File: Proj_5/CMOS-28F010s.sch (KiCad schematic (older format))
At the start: 5 parts, among them U12 28F010, U13 PAL16L8, U4 28F010

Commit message: Sick wires bro
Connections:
- net A17: now also U13.3 (I3); no longer U13.17 (I03)
- net A18: now also U13.2 (I2); no longer U13.18 (IO2)
- net A19: now also U13.1 (I1); no longer U13.19 (IO1)
- net ~BHE: now also U13.5 (I5); no longer U13.15 (IO5)
- net ~BLE: now also U13.4 (I4); no longer U13.16 (IO4)
- net at U12.22 (CE): now also U13.18 (IO2); no longer U13.2 (I2)
- net at U4.22 (CE): now also U13.19 (IO1); no longer U13.1 (I1)
- net M~IO: now reaches U13.6 (I6)
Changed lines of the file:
@@
 $Descr User 15748 23622
 encoding utf-8
-Sheet 8 9
+Sheet 7 9
 Title ""
 Date ""
@@
 F 3 "" H 10350 4550 50  0001 C CNN
 	1    10350 4550
-	1    0    0    -1
+	-1   0    0    -1
 $EndComp
 Text HLabel 10850 4050 2    50   Input ~ 0
@@
 Text HLabel 7350 2900 2    50   Input ~ 0
 A14
+Text HLabel 10850 4550 2    50   Input ~ 0
+M~IO
 $EndSCHEMATC

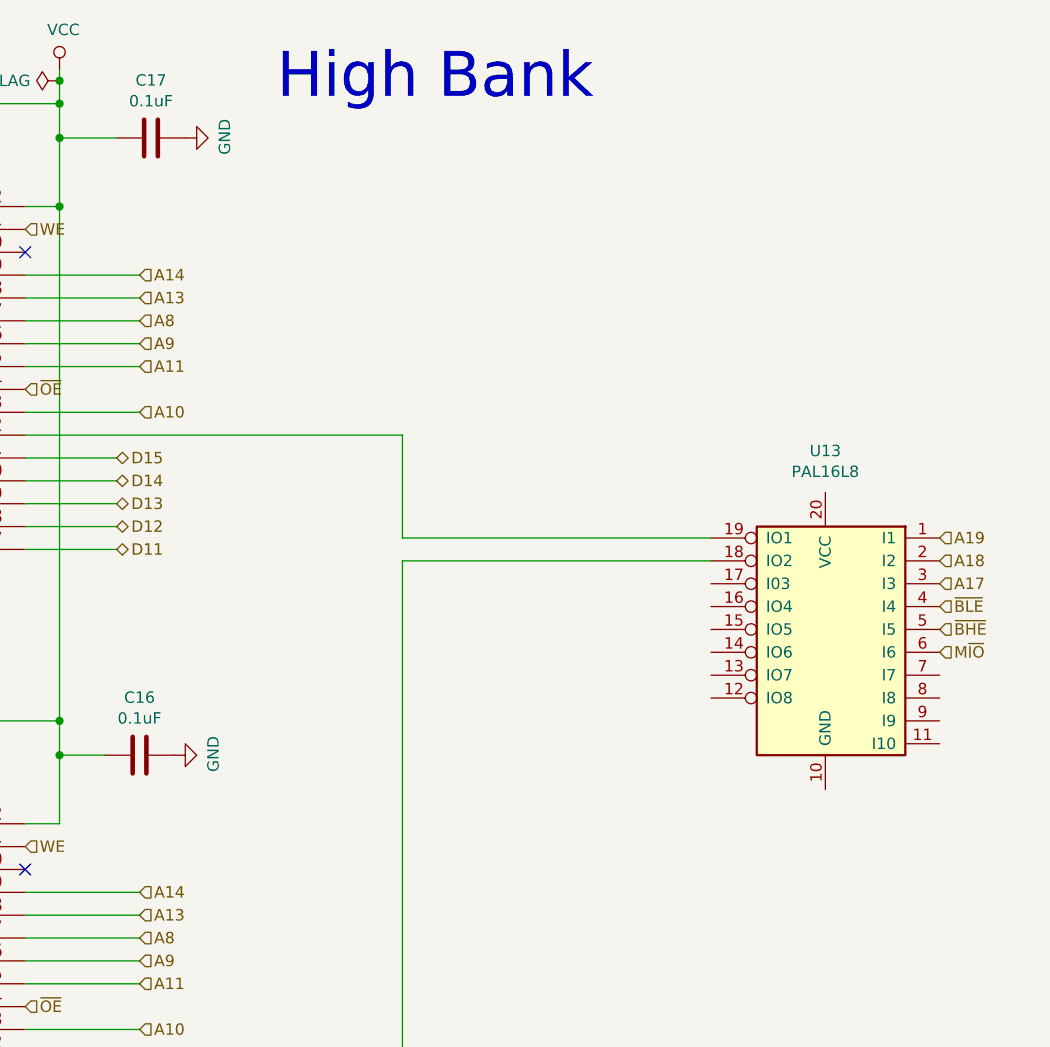
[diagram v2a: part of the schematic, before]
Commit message: Added Power Flags, finished no connects.
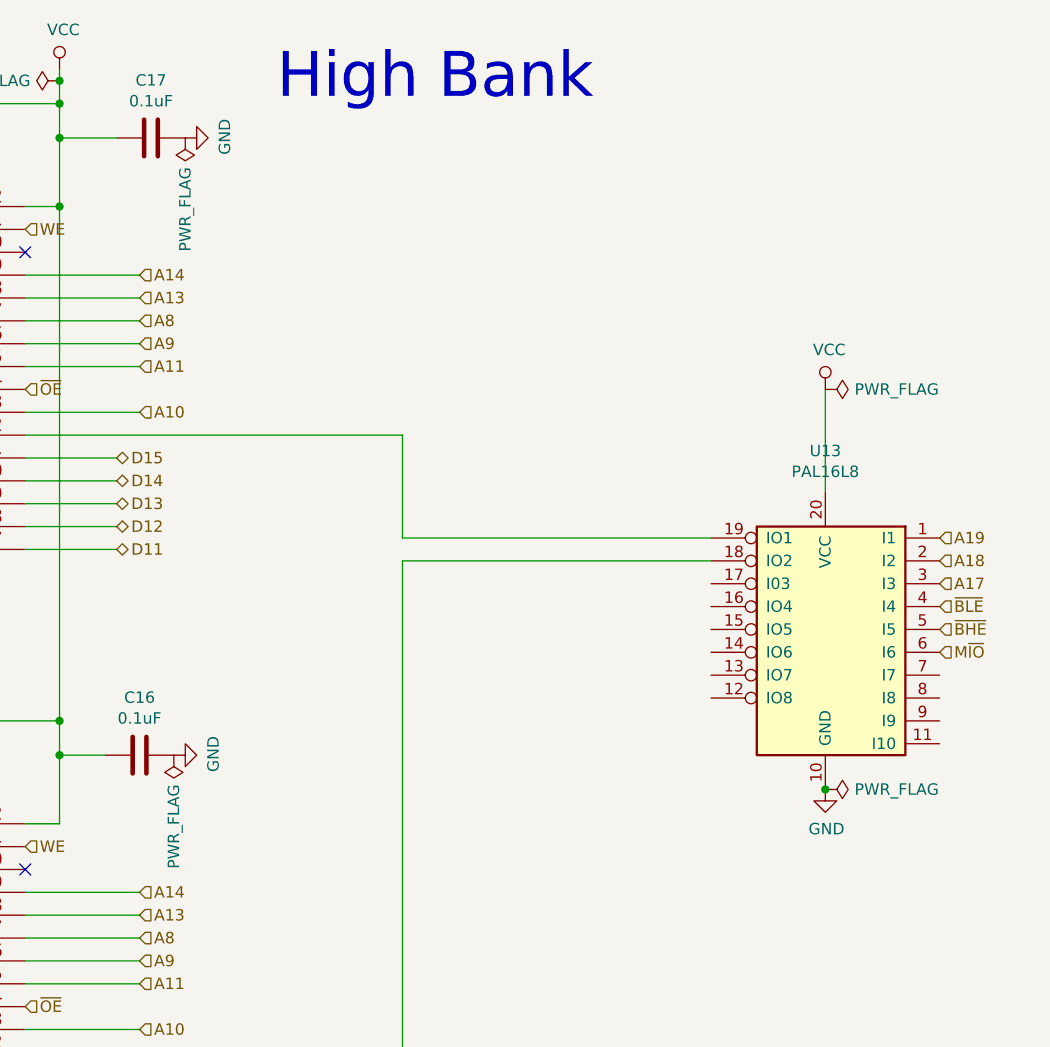
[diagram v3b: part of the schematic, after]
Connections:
- net GND: now also U13.10 (GND)
- net VCC: now also U13.20 (VCC)
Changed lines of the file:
@@
 $Descr User 15748 23622
 encoding utf-8
-Sheet 5 9
+Sheet 5 10
 Title ""
 Date ""
@@
 Text HLabel 10850 4550 2    50   Input ~ 0
 M~IO
+$Comp
+L power:PWR_FLAG #FLG?
+U 1 1 5F396526
+P 7500 5000
+AR Path="/5EAF7226/5F396526" Ref="#FLG?"  Part="1"
+AR Path="/5EA045EA/5F396526" Ref="#FLG041"  Part="1"
+F 0 "#FLG041" H 7500 5075 50  0001 C CNN
+F 1 "PWR_FLAG" V 7500 5128 50  0000 L CNN
+F 2 "" H 7500 5000 50  0001 C CNN
+F 3 "~" H 7500 5000 50  0001 C CNN
+	1    7500 5000
+	-1   0    0    1
+$EndComp
+$Comp
+L power:PWR_FLAG #FLG?
+U 1 1 5F398AC0
+P 7550 2300
+AR Path="/5EAF7226/5F398AC0" Ref="#FLG?"  Part="1"
+AR Path="/5EA045EA/5F398AC0" Ref="#FLG042"  Part="1"
+F 0 "#FLG042" H 7550 2375 50  0001 C CNN
+F 1 "PWR_FLAG" V 7550 2428 50  0000 L CNN
+F 2 "" H 7550 2300 50  0001 C CNN
+F 3 "~" H 7550 2300 50  0001 C CNN
+	1    7550 2300
+	-1   0    0    1
+$EndComp
+$Comp
+L power:PWR_FLAG #FLG?
+U 1 1 5F39F13F
+P 10350 5150
+AR Path="/5EAF7226/5F39F13F" Ref="#FLG?"  Part="1"
+AR Path="/5EA045EA/5F39F13F" Ref="#FLG044"  Part="1"
+F 0 "#FLG044" H 10350 5225 50  0001 C CNN
+F 1 "PWR_FLAG" V 10350 5278 50  0000 L CNN
+F 2 "" H 10350 5150 50  0001 C CNN
+F 3 "~" H 10350 5150 50  0001 C CNN
+	1    10350 5150
+	0    1    1    0
+$EndComp
+$Comp
+L power:GND #PWR047
+U 1 1 5F3A169C
+P 10350 5150
+AR Path="/5EA045EA/5F3A169C" Ref="#PWR047"  Part="1"
+AR Path="/5EA98353/5EA34234/5F3A169C" Ref="#PWR?"  Part="1"
+F 0 "#PWR047" H 10350 4900 50  0001 C CNN
+F 1 "GND" H 10355 4977 50  0000 C CNN
+F 2 "" H 10350 5150 50  0001 C CNN
+F 3 "" H 10350 5150 50  0001 C CNN
+	1    10350 5150
+	1    0    0    -1
+$EndComp
+Connection ~ 10350 5150
+$Comp
+L power:VCC #PWR046
+U 1 1 5F3AB457
+P 10350 3400
+AR Path="/5EA045EA/5F3AB457" Ref="#PWR046"  Part="1"
+AR Path="/5EA98353/5EA34234/5F3AB457" Ref="#PWR?"  Part="1"
+F 0 "#PWR046" H 10350 3250 50  0001 C CNN
+F 1 "VCC" H 10367 3573 50  0000 C CNN
+F 2 "" H 10350 3400 50  0001 C CNN
+F 3 "" H 10350 3400 50  0001 C CNN
+	1    10350 3400
+	1    0    0    -1
+$EndComp
+Wire Wire Line
+	10350 3400 10350 3850
+$Comp
+L power:PWR_FLAG #FLG?
+U 1 1 5F3B0971
+P 10350 3400
+AR Path="/5EAF7226/5F3B0971" Ref="#FLG?"  Part="1"
+AR Path="/5EA045EA/5F3B0971" Ref="#FLG043"  Part="1"
+F 0 "#FLG043" H 10350 3475 50  0001 C CNN
+F 1 "PWR_FLAG" V 10350 3528 50  0000 L CNN
+F 2 "" H 10350 3400 50  0001 C CNN
+F 3 "~" H 10350 3400 50  0001 C CNN
+	1    10350 3400
+	0    1    1    0
+$EndComp
 $EndSCHEMATC

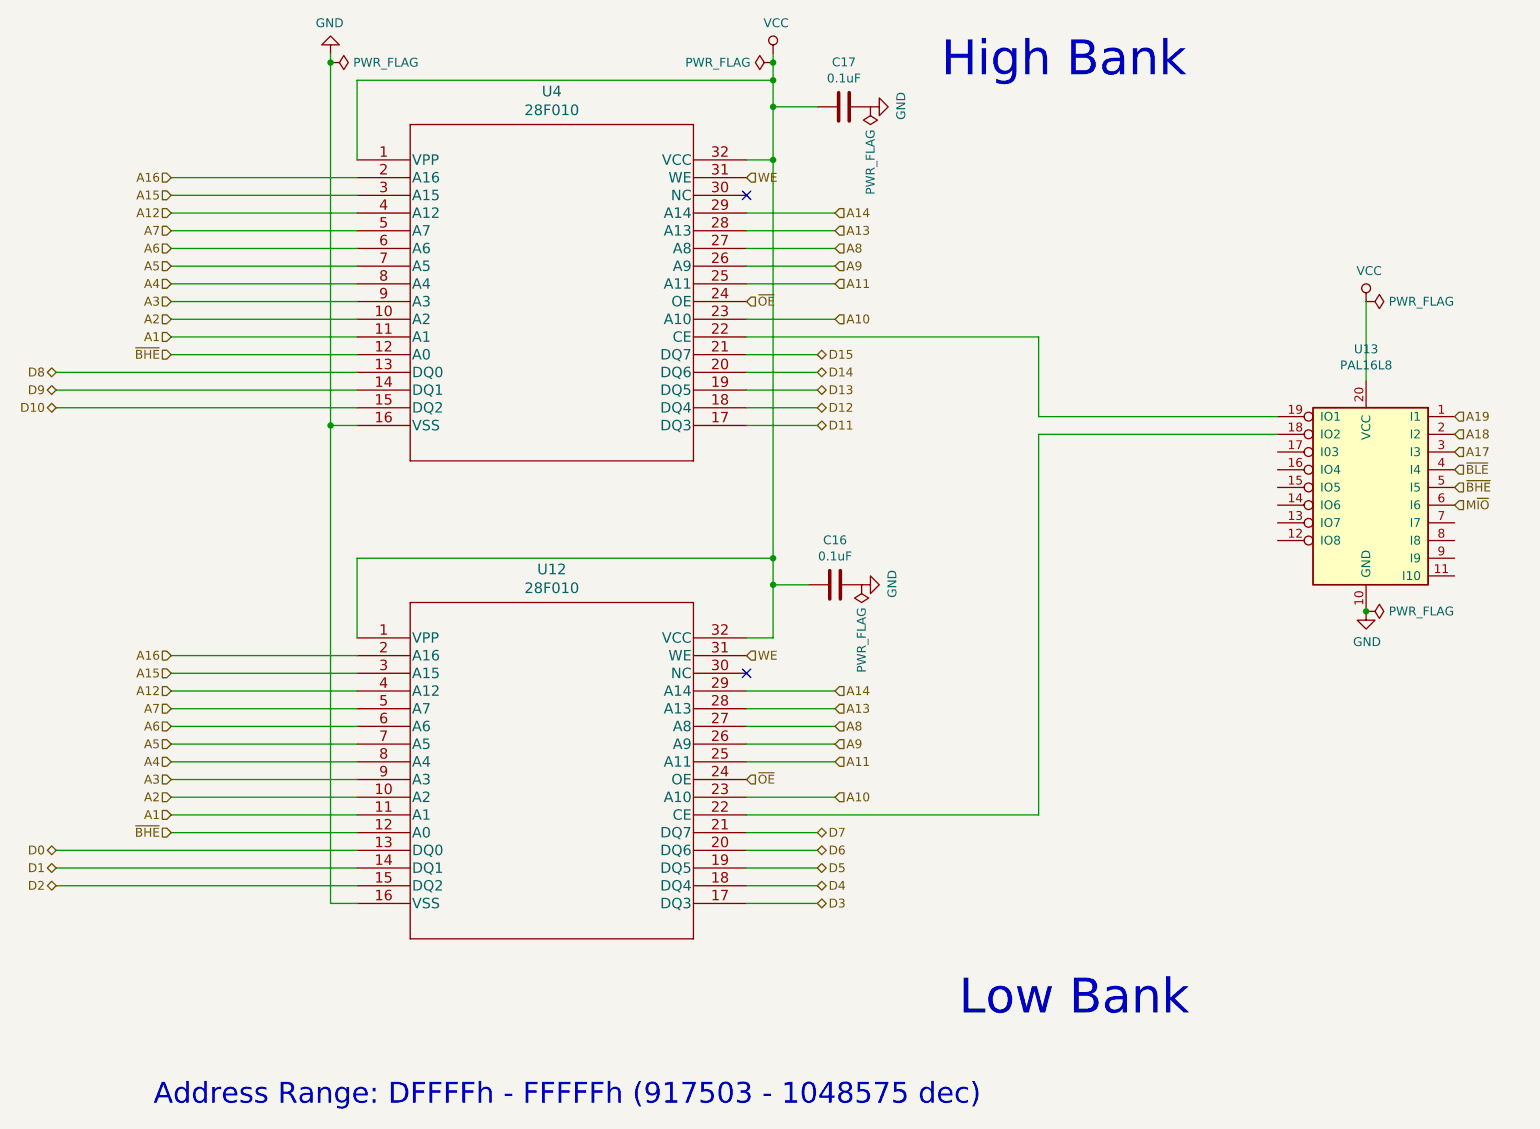
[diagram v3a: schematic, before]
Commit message: Power Flags
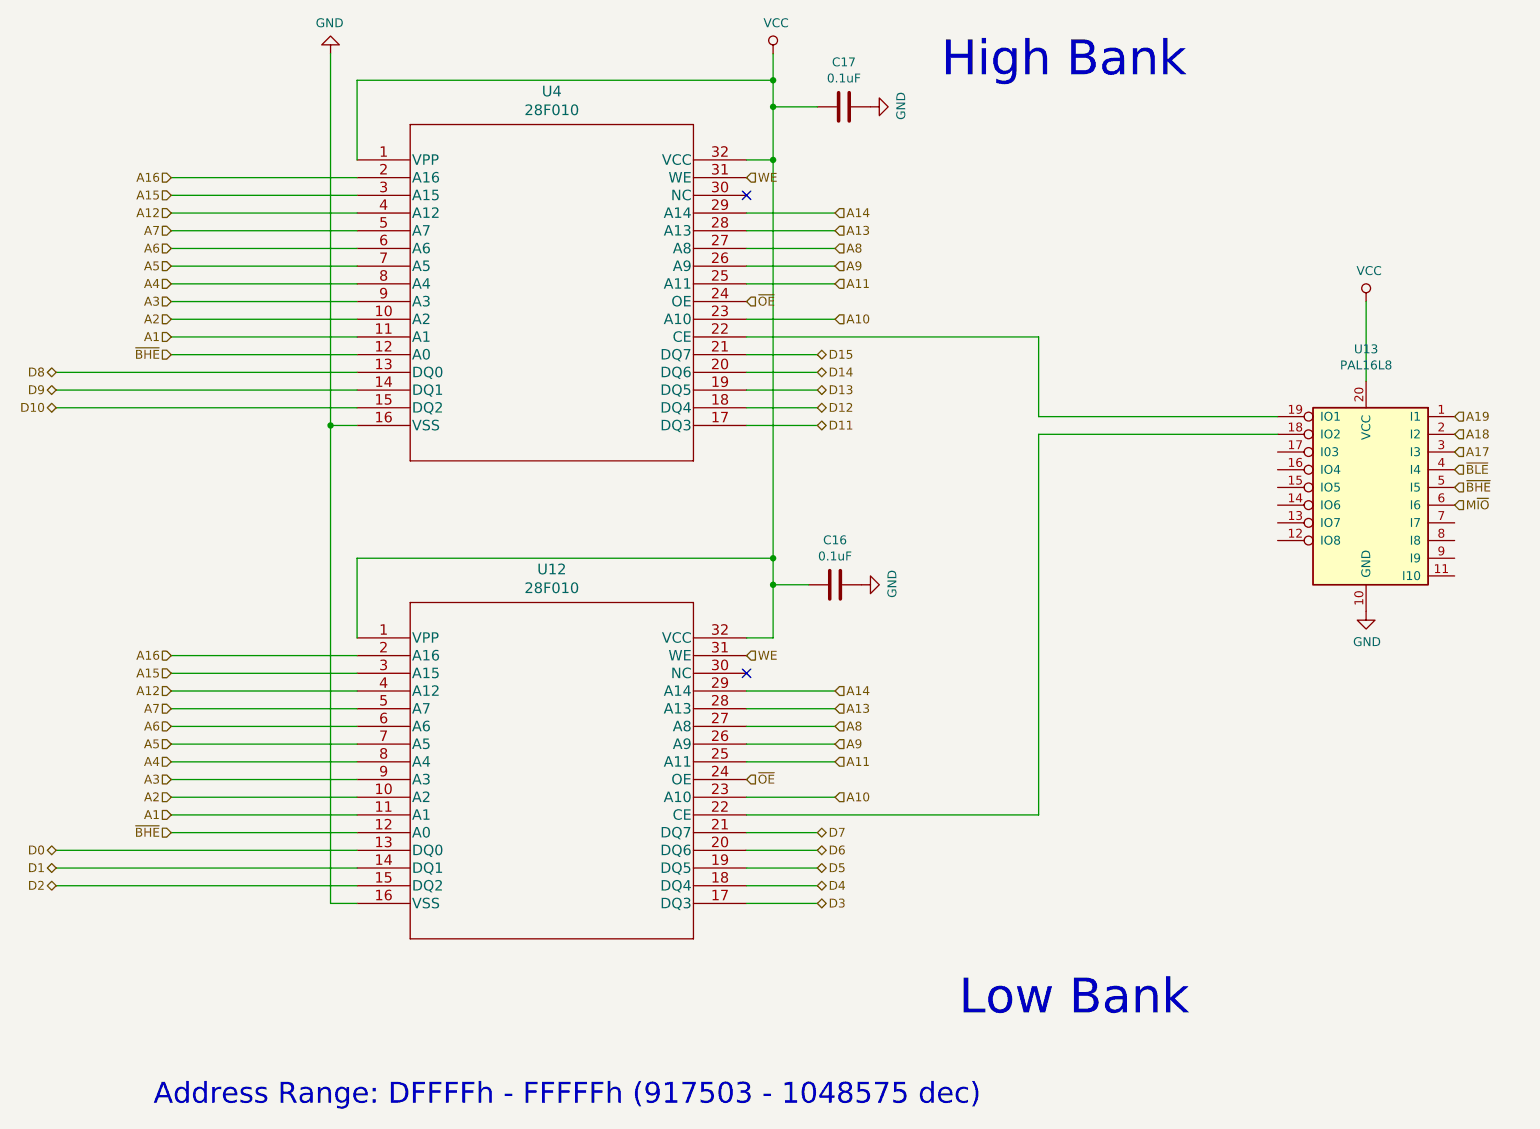
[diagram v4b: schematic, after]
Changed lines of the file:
@@
 $Descr User 15748 23622
 encoding utf-8
-Sheet 5 10
+Sheet 4 10
 Title ""
 Date ""
@@
 	2950 4000 4650 4000
 Wire Wire Line
-	7000 2000 7000 2050
-Wire Wire Line
 	6850 2600 7000 2600
 $Comp
@@
 	-1   0    0    1
 $EndComp
-Wire Wire Line
-	4500 2000 4500 2050
 Wire Wire Line
 	4500 4100 4650 4100
@@
 	1    0    0    -1
 $EndComp
-$Comp
-L power:PWR_FLAG #FLG0103
-U 1 1 5EBED100
-P 4500 2050
-AR Path="/5EA045EA/5EBED100" Ref="#FLG0103"  Part="1"
-AR Path="/5EA98353/5EA34234/5EBED100" Ref="#FLG?"  Part="1"
-F 0 "#FLG0103" H 4500 2125 50  0001 C CNN
-F 1 "PWR_FLAG" V 4500 2178 50  0000 L CNN
-F 2 "" H 4500 2050 50  0001 C CNN
-F 3 "~" H 4500 2050 50  0001 C CNN
-	1    4500 2050
-	0    1    1    0
-$EndComp
-Connection ~ 4500 2050
-Wire Wire Line
-	4500 2050 4500 4100
-$Comp
-L power:PWR_FLAG #FLG0104
-U 1 1 5EBEE814
-P 7000 2050
-AR Path="/5EA045EA/5EBEE814" Ref="#FLG0104"  Part="1"
-AR Path="/5EA98353/5EA34234/5EBEE814" Ref="#FLG?"  Part="1"
-F 0 "#FLG0104" H 7000 2125 50  0001 C CNN
-F 1 "PWR_FLAG" V 7000 2177 50  0000 L CNN
-F 2 "" H 7000 2050 50  0001 C CNN
-F 3 "~" H 7000 2050 50  0001 C CNN
-	1    7000 2050
-	0    -1   -1   0
-$EndComp
 Wire Wire Line
 	7000 2150 4650 2150
@@
 Wire Wire Line
 	7000 2150 7000 2300
-Connection ~ 7000 2050
-Wire Wire Line
-	7000 2050 7000 2150
 Wire Wire Line
 	3600 5400 4650 5400
@@
 M~IO
 $Comp
-L power:PWR_FLAG #FLG?
-U 1 1 5F396526
-P 7500 5000
-AR Path="/5EAF7226/5F396526" Ref="#FLG?"  Part="1"
-AR Path="/5EA045EA/5F396526" Ref="#FLG041"  Part="1"
-F 0 "#FLG041" H 7500 5075 50  0001 C CNN
-F 1 "PWR_FLAG" V 7500 5128 50  0000 L CNN
-F 2 "" H 7500 5000 50  0001 C CNN
-F 3 "~" H 7500 5000 50  0001 C CNN
-	1    7500 5000
-	-1   0    0    1
-$EndComp
-$Comp
-L power:PWR_FLAG #FLG?
-U 1 1 5F398AC0
-P 7550 2300
-AR Path="/5EAF7226/5F398AC0" Ref="#FLG?"  Part="1"
-AR Path="/5EA045EA/5F398AC0" Ref="#FLG042"  Part="1"
-F 0 "#FLG042" H 7550 2375 50  0001 C CNN
-F 1 "PWR_FLAG" V 7550 2428 50  0000 L CNN
-F 2 "" H 7550 2300 50  0001 C CNN
-F 3 "~" H 7550 2300 50  0001 C CNN
-	1    7550 2300
-	-1   0    0    1
-$EndComp
-$Comp
-L power:PWR_FLAG #FLG?
-U 1 1 5F39F13F
-P 10350 5150
-AR Path="/5EAF7226/5F39F13F" Ref="#FLG?"  Part="1"
-AR Path="/5EA045EA/5F39F13F" Ref="#FLG044"  Part="1"
-F 0 "#FLG044" H 10350 5225 50  0001 C CNN
-F 1 "PWR_FLAG" V 10350 5278 50  0000 L CNN
-F 2 "" H 10350 5150 50  0001 C CNN
-F 3 "~" H 10350 5150 50  0001 C CNN
-	1    10350 5150
-	0    1    1    0
-$EndComp
-$Comp
 L power:GND #PWR047
 U 1 1 5F3A169C
@@
 	1    0    0    -1
 $EndComp
-Connection ~ 10350 5150
 $Comp
 L power:VCC #PWR046
@@
 Wire Wire Line
 	10350 3400 10350 3850
-$Comp
-L power:PWR_FLAG #FLG?
-U 1 1 5F3B0971
-P 10350 3400
-AR Path="/5EAF7226/5F3B0971" Ref="#FLG?"  Part="1"
-AR Path="/5EA045EA/5F3B0971" Ref="#FLG043"  Part="1"
-F 0 "#FLG043" H 10350 3475 50  0001 C CNN
-F 1 "PWR_FLAG" V 10350 3528 50  0000 L CNN
-F 2 "" H 10350 3400 50  0001 C CNN
-F 3 "~" H 10350 3400 50  0001 C CNN
-	1    10350 3400
-	0    1    1    0
-$EndComp
+Wire Wire Line
+	4500 2000 4500 4100
+Wire Wire Line
+	7000 2000 7000 2150
 $EndSCHEMATC

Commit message: Destroyed errors
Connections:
- net ~BHE: no longer U12.12 (A0)
- net ~BLE: now also U12.12 (A0)
- no-connect marks 2 -> 12
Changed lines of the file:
@@
 Wire Wire Line
 	8500 4150 8500 6300
-Text HLabel 3600 6400 0    50   Input ~ 0
-~BHE
 Text HLabel 3600 6300 0    50   Input ~ 0
 A1
@@
 Wire Wire Line
 	7000 2000 7000 2150
+NoConn ~ 9850 4250
+NoConn ~ 9850 4350
+NoConn ~ 9850 4450
+NoConn ~ 9850 4550
+NoConn ~ 9850 4650
+NoConn ~ 9850 4750
+NoConn ~ 10850 4650
+NoConn ~ 10850 4750
+NoConn ~ 10850 4850
+NoConn ~ 10850 4950
+Text HLabel 3600 6400 0    50   Input ~ 0
+~BLE
 $EndSCHEMATC

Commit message: 11 errors left
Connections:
- net M~IO: now also U13.4 (I4); no longer U13.6 (I6)
- net ~BHE: no longer U13.5 (I5)
- net ~BLE: no longer U13.4 (I4)
- no-connect marks 12 -> 14
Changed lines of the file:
@@
 Text HLabel 6850 5400 2    50   Input ~ 0
 WE
-Text HLabel 6850 3400 2    50   Input ~ 0
+Text HLabel 7100 3400 2    50   Input ~ 0
 ~OE
-Text HLabel 6850 6100 2    50   Input ~ 0
+Text HLabel 7000 6100 2    50   Input ~ 0
 ~OE
 $Comp
@@
 Text HLabel 10850 4250 2    50   Input ~ 0
 A17
-Text HLabel 10850 4350 2    50   Input ~ 0
-~BLE
-Text HLabel 10850 4450 2    50   Input ~ 0
-~BHE
 Wire Wire Line
 	9850 4050 8500 4050
@@
 Text HLabel 7350 2900 2    50   Input ~ 0
 A14
-Text HLabel 10850 4550 2    50   Input ~ 0
+Text HLabel 10850 4350 2    50   Input ~ 0
 M~IO
 $Comp
@@
 Text HLabel 3600 6400 0    50   Input ~ 0
 ~BLE
+NoConn ~ 10850 4450
+NoConn ~ 10850 4550
+Wire Wire Line
+	6850 3400 7100 3400
+Wire Wire Line
+	6850 6100 7000 6100
 $EndSCHEMATC

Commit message: Added 5 Footprints
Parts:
- U12: footprint 28F010 -> (none)
- U4: footprint 28F010 -> parts:28F010
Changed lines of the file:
@@
 F 0 "U4" H 5750 2987 60  0000 C CNN
 F 1 "28F010" H 5750 2881 60  0000 C CNN
-F 2 "28F010" H 5750 2840 60  0001 C CNN
+F 2 "parts:28F010" H 5750 2840 60  0001 C CNN
 F 3 "" H 4650 2600 60  0000 C CNN
 	1    4650 2600
@@
 F 0 "U12" H 5750 5687 60  0000 C CNN
 F 1 "28F010" H 5750 5581 60  0000 C CNN
-F 2 "28F010" H 5750 5540 60  0001 C CNN
+F 2 "" H 5750 5540 60  0001 C CNN
 F 3 "" H 4650 5300 60  0000 C CNN
 	1    4650 5300

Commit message: Added at least 4 Footprints
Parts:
- C16, C17: footprint (none) -> Capacitor_Tantalum_SMD:CP_EIA-1608-08_AVX-J
- U12: footprint (none) -> parts:28F010
- U13: footprint (none) -> Package_DIP:DIP-20_W7.62mm
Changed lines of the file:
@@
 F 0 "U12" H 5750 5687 60  0000 C CNN
 F 1 "28F010" H 5750 5581 60  0000 C CNN
-F 2 "" H 5750 5540 60  0001 C CNN
+F 2 "parts:28F010" H 5750 5540 60  0001 C CNN
 F 3 "" H 4650 5300 60  0000 C CNN
 	1    4650 5300
@@
 F 0 "C17" V 7148 2300 50  0000 C CNN
 F 1 "0.1uF" V 7239 2300 50  0000 C CNN
-F 2 "" H 7438 2150 50  0001 C CNN
+F 2 "Capacitor_Tantalum_SMD:CP_EIA-1608-08_AVX-J" H 7438 2150 50  0001 C CNN
 F 3 "~" H 7400 2300 50  0001 C CNN
 	1    7400 2300
@@
 F 0 "C16" V 7098 5000 50  0000 C CNN
 F 1 "0.1uF" V 7189 5000 50  0000 C CNN
-F 2 "" H 7388 4850 50  0001 C CNN
+F 2 "Capacitor_Tantalum_SMD:CP_EIA-1608-08_AVX-J" H 7388 4850 50  0001 C CNN
 F 3 "~" H 7350 5000 50  0001 C CNN
 	1    7350 5000
@@
 F 0 "U13" H 10350 5431 50  0000 C CNN
 F 1 "PAL16L8" H 10350 5340 50  0000 C CNN
-F 2 "" H 10350 4550 50  0001 C CNN
+F 2 "Package_DIP:DIP-20_W7.62mm" H 10350 4550 50  0001 C CNN
 F 3 "" H 10350 4550 50  0001 C CNN
 	1    10350 4550
